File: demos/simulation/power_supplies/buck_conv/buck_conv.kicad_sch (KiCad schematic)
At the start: 8 parts, among them Q1 IRF540N

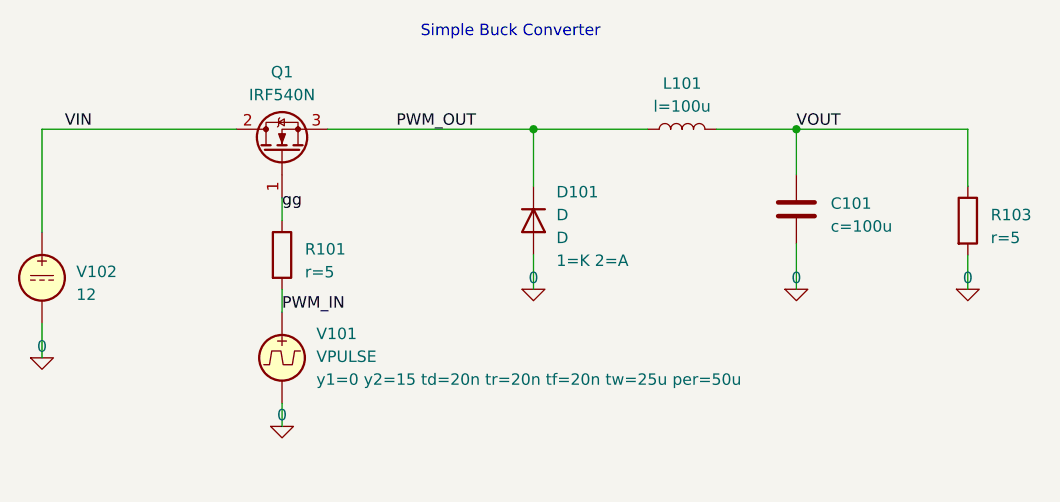
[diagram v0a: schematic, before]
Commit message: Update simulation demos: Replace '0' symbols with GND
Just a tiny visual fix: Replace the 0-Symbol with GND symbol.
Also store as KiCad9
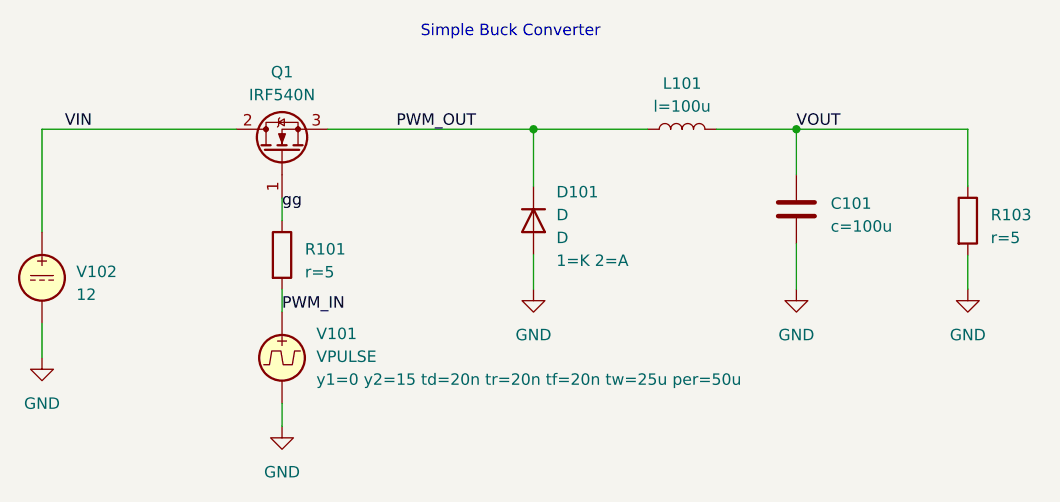
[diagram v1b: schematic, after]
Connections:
- net 0 renamed GND
